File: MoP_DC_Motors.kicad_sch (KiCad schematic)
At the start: 21 parts, among them J18 Encoder1, J19 Encoder2, M3 1x2_Terminal, M4 1x2_Terminal, U4 L293D, U5 74AHCT1G14, U6 74AHCT1G14

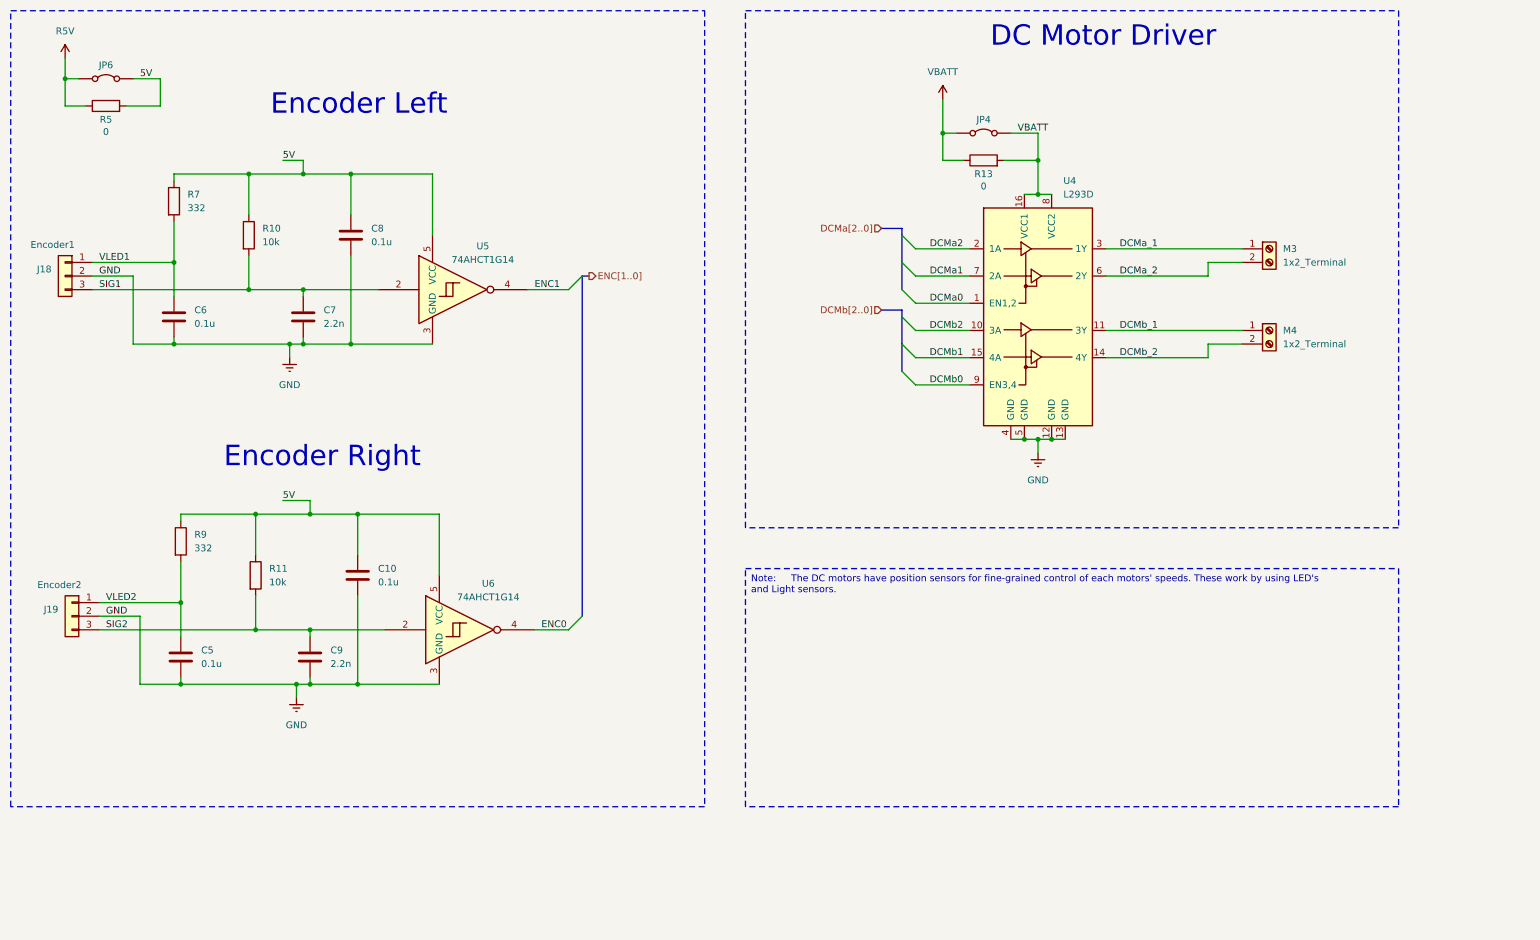
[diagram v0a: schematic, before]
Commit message: changed ref designators to be consistent accross sheets
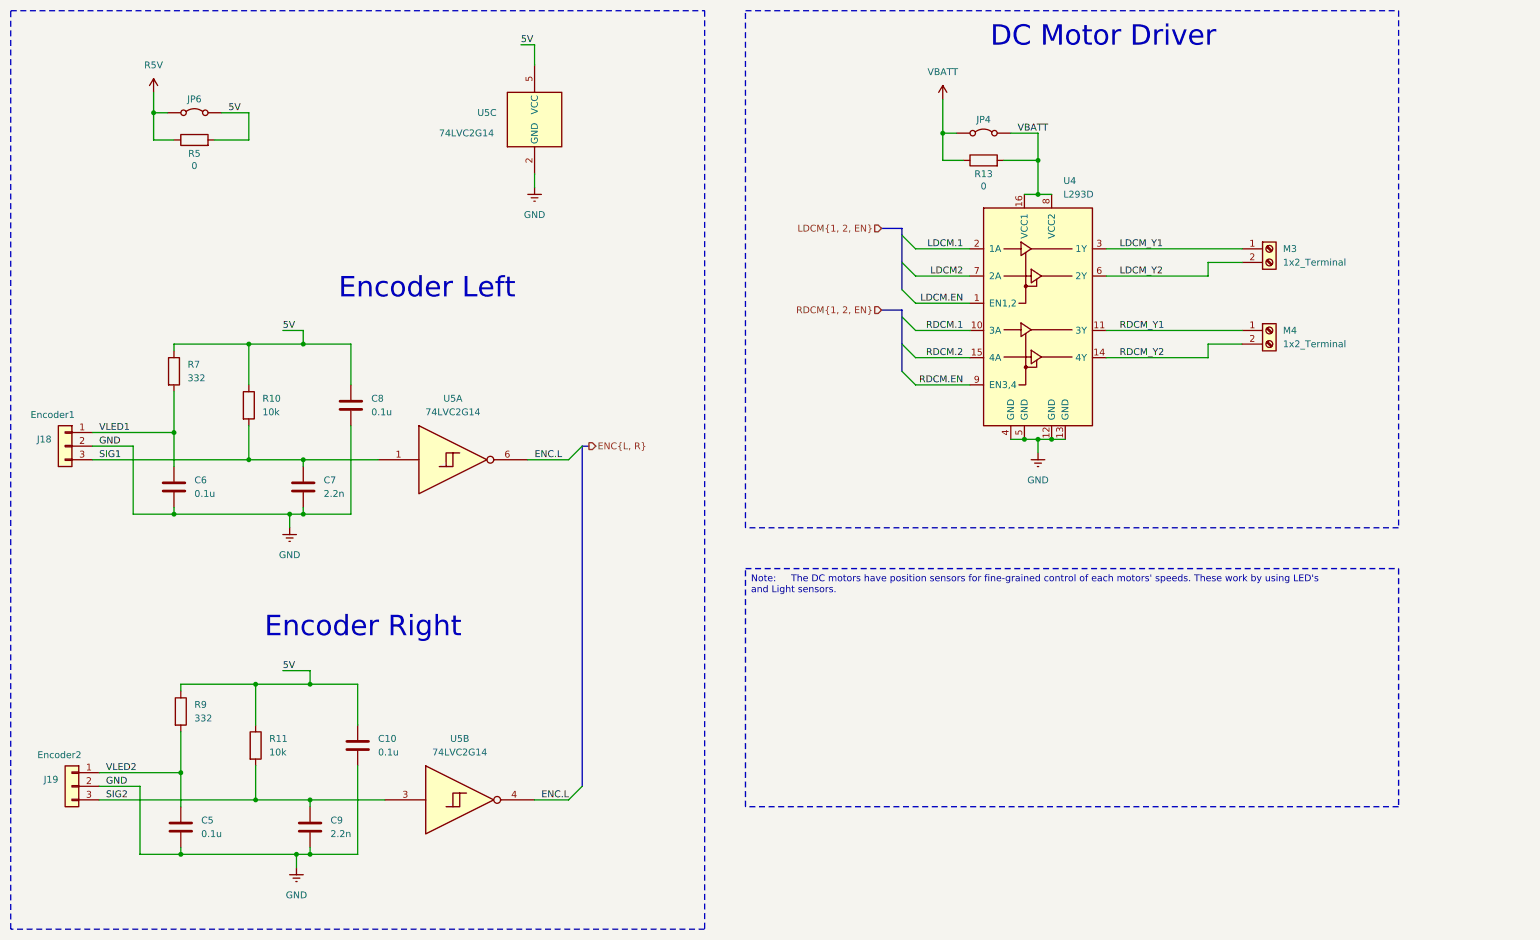
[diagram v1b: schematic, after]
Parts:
- removed U5, U6: 74AHCT1G14, symbol 74xGxx:74AHCT1G14
- added U5: 74LVC2G14, Package_TO_SOT_SMD:SOT-23-6, symbol 74xGxx:74LVC2G14
- C6, C7, C8: footprint (none) -> Capacitor_SMD:C_0805_2012Metric_Pad1.18x1.45mm_HandSolder
- R10, R7: footprint (none) -> Resistor_SMD:R_0805_2012Metric
- U4: footprint Package_DIP:DIP-20_W7.62mm_SMDSocket_SmallPads -> Package_DIP:DIP-16_W7.62mm_LongPads
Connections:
- net 5V: now also U5.5 (VCC)
- net GND: now also U5.2 (GND)
- net SIG1: now also U5.1
- net SIG2: now also U5.3
- net DCMa0 renamed LDCM.EN
- net DCMa1 renamed LDCM2
- net DCMa2 renamed LDCM.1
- net DCMa_1 renamed LDCM_Y1
- net DCMa_2 renamed LDCM_Y2
- net DCMb0 renamed RDCM.EN
- net DCMb1 renamed RDCM.2
- net DCMb2 renamed RDCM.1
- net DCMb_1 renamed RDCM_Y1
- net DCMb_2 renamed RDCM_Y2
- new net ENC.L: U5.4, U5.6
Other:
- moved on the sheet: C10, C5, C6, C7, C8, C9, J18, J19, JP6, R10, R11, R5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

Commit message: Finished schematics
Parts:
- C504: renamed from C10; footprint (none) -> Capacitor_SMD:C_0805_2012Metric_Pad1.18x1.45mm_HandSolder
- C505: renamed from C5; footprint (none) -> Capacitor_SMD:C_0805_2012Metric_Pad1.18x1.45mm_HandSolder
- C506: renamed from C9; footprint (none) -> Capacitor_SMD:C_0805_2012Metric_Pad1.18x1.45mm_HandSolder
- J501: renamed from J18; footprint (none) -> Connector_PinHeader_2.54mm:PinHeader_1x03_P2.54mm_Vertical
- J502: renamed from J19; footprint (none) -> Connector_PinHeader_2.54mm:PinHeader_1x03_P2.54mm_Vertical
- J503: renamed from M3; footprint (none) -> TerminalBlock_Phoenix:TerminalBlock_Phoenix_MKDS-1,5-2-5.08_1x02_P5.08mm_Horizontal
- J504: renamed from M4; footprint (none) -> TerminalBlock_Phoenix:TerminalBlock_Phoenix_MKDS-1,5-2-5.08_1x02_P5.08mm_Horizontal
- JP501: renamed from JP6; footprint (none) -> Connector_PinHeader_2.54mm:PinHeader_1x02_P2.54mm_Vertical
- JP502: renamed from JP4; footprint (none) -> Connector_PinHeader_2.54mm:PinHeader_1x02_P2.54mm_Vertical
- R501: renamed from R5; footprint (none) -> Resistor_SMD:R_0805_2012Metric; now not fitted
- R504: renamed from R9; footprint (none) -> Resistor_SMD:R_0805_2012Metric
- R505: renamed from R11; footprint (none) -> Resistor_SMD:R_0805_2012Metric
- R506: renamed from R13; footprint (none) -> Resistor_SMD:R_0805_2012Metric; now not fitted
- U4: footprint Package_DIP:DIP-16_W7.62mm_LongPads -> Package_DIP:DIP-16_W7.62mm_Socket_LongPads
- renumbered C8 to C501, C6 to C502, C7 to C503, R7 to R502, R10 to R503, U5 to U501
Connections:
- net VBATT: no longer JP502.2 (B), R506.2, U4.16 (VCC1), U4.8 (VCC2)
- new net VS: JP502.2 (B), R506.2, U4.16 (VCC1), U4.8 (VCC2)
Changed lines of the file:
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@@
 		)
 	)
-	(text_box "Note: 	The DC motors have position sensors for fine-grained control of each motors' speeds. These work by using LED's and Light sensors."
+	(text_box "Note: 	The DC motors have position sensors for fine-grained control of each motors' speeds. These work by using \n		LED's and Light sensors.\n\n		The L293D is a DIP-16 package that is installed via socket"
 		(exclude_from_sim no)
 		(at 156.21 123.19 0)
@@
 		)
 	)
-	(label "VBATT"
+	(label "VS"
 		(at 207.01 41.91 0)
 		(fields_autoplaced yes)
@@
 		(dnp no)
 		(fields_autoplaced yes)
-		(property "Reference" "R7"
+		(property "Reference" "R502"
 			(at 52.07 85.0899 0)
 			(effects
@@
 			(project "MoP"
 				(path "/4d76798e-9a11-4d8d-a723-72f274a89091/35a0f4f1-9888-4ee1-94e1-e8485c96600c"
-					(reference "R7")
+					(reference "R502")
 					(unit 1)
 				)
@@
 		(dnp no)
 		(fields_autoplaced yes)
-		(property "Reference" "C6"
+		(property "Reference" "C502"
 			(at 53.34 106.6799 0)
 			(effects
@@
 			(project "MoP"
 				(path "/4d76798e-9a11-4d8d-a723-72f274a89091/35a0f4f1-9888-4ee1-94e1-e8485c96600c"
-					(reference "C6")
+					(reference "C502")
 					(unit 1)
 				)
@@
 		(dnp no)
 		(fields_autoplaced yes)
-		(property "Reference" "R10"
+		(property "Reference" "R503"
 			(at 66.04 91.4399 0)
 			(effects
@@
 			(project "MoP"
 				(path "/4d76798e-9a11-4d8d-a723-72f274a89091/35a0f4f1-9888-4ee1-94e1-e8485c96600c"
-					(reference "R10")
+					(reference "R503")
 					(unit 1)
 				)
@@
 		(on_board yes)
 		(dnp no)
-		(property "Reference" "U5"
+		(property "Reference" "U501"
 			(at 107.95 38.1 0)
 			(effects
@@
 			(project "MoP"
 				(path "/4d76798e-9a11-4d8d-a723-72f274a89091/35a0f4f1-9888-4ee1-94e1-e8485c96600c"
-					(reference "U5")
+					(reference "U501")
 					(unit 3)
 				)
@@
 		(exclude_from_sim no)
 		(in_bom yes)
-		(on_board yes)
-		(dnp no)
-		(property "Reference" "R5"
+		(on_board no)
+		(dnp yes)
+		(property "Reference" "R501"
 			(at 53.34 45.72 90)
 			(effects
@@
 			)
 		)
-		(property "Footprint" ""
+		(property "Footprint" "Resistor_SMD:R_0805_2012Metric"
 			(at 53.34 44.958 90)
 			(effects
@@
 			(project "MoP"
 				(path "/4d76798e-9a11-4d8d-a723-72f274a89091/35a0f4f1-9888-4ee1-94e1-e8485c96600c"
-					(reference "R5")
+					(reference "R501")
 					(unit 1)
 				)
@@
 		(dnp no)
 		(fields_autoplaced yes)
-		(property "Reference" "U5"
+		(property "Reference" "U501"
 			(at 101.6 91.44 0)
 			(effects
@@
 			(project "MoP"
 				(path "/4d76798e-9a11-4d8d-a723-72f274a89091/35a0f4f1-9888-4ee1-94e1-e8485c96600c"
-					(reference "U5")
+					(reference "U501")
 					(unit 1)
 				)
@@
 		(dnp no)
 		(fields_autoplaced yes)
-		(property "Reference" "C5"
+		(property "Reference" "C505"
 			(at 54.61 170.1799 0)
 			(effects
@@
 			)
 		)
-		(property "Footprint" ""
+		(property "Footprint" "Capacitor_SMD:C_0805_2012Metric_Pad1.18x1.45mm_HandSolder"
 			(at 51.7652 175.26 0)
 			(effects
@@
 			(project "MoP"
 				(path "/4d76798e-9a11-4d8d-a723-72f274a89091/35a0f4f1-9888-4ee1-94e1-e8485c96600c"
-					(reference "C5")
+					(reference "C505")
 					(unit 1)
 				)
@@
 		(dnp no)
 		(fields_autoplaced yes)
-		(property "Reference" "M3"
+		(property "Reference" "J503"
 			(at 256.54 63.4999 0)
 			(effects
@@
 			)
 		)
-		(property "Footprint" ""
+		(property "Footprint" "TerminalBlock_Phoenix:TerminalBlock_Phoenix_MKDS-1,5-2-5.08_1x02_P5.08mm_Horizontal"
 			(at 254 63.5 0)
 			(effects
@@
 			(project "MoP"
 				(path "/4d76798e-9a11-4d8d-a723-72f274a89091/35a0f4f1-9888-4ee1-94e1-e8485c96600c"
-					(reference "M3")
+					(reference "J503")
 					(unit 1)
 				)
@@
 		(dnp no)
 		(fields_autoplaced yes)
-		(property "Reference" "JP4"
+		(property "Reference" "JP502"
 			(at 200.66 39.37 0)
 			(effects
@@
 			)
 		)
-		(property "Footprint" ""
+		(property "Footprint" "Connector_PinHeader_2.54mm:PinHeader_1x02_P2.54mm_Vertical"
 			(at 200.66 41.91 0)
 			(effects
@@
 			(project "MoP"
 				(path "/4d76798e-9a11-4d8d-a723-72f274a89091/35a0f4f1-9888-4ee1-94e1-e8485c96600c"
-					(reference "JP4")
+					(reference "JP502")
 					(unit 1)
 				)
@@
 		(dnp no)
 		(fields_autoplaced yes)
-		(property "Reference" "M4"
+		(property "Reference" "J504"
 			(at 256.54 78.7399 0)
 			(effects
@@
 			)
 		)
-		(property "Footprint" ""
+		(property "Footprint" "TerminalBlock_Phoenix:TerminalBlock_Phoenix_MKDS-1,5-2-5.08_1x02_P5.08mm_Horizontal"
 			(at 254 78.74 0)
 			(effects
@@
 			(project "MoP"
 				(path "/4d76798e-9a11-4d8d-a723-72f274a89091/35a0f4f1-9888-4ee1-94e1-e8485c96600c"
-					(reference "M4")
+					(reference "J504")
 					(unit 1)
 				)
@@
 		(dnp no)
 		(fields_autoplaced yes)
-		(property "Reference" "C8"
+		(property "Reference" "C501"
 			(at 86.36 91.4399 0)
 			(effects
@@
 			(project "MoP"
 				(path "/4d76798e-9a11-4d8d-a723-72f274a89091/35a0f4f1-9888-4ee1-94e1-e8485c96600c"
-					(reference "C8")
+					(reference "C501")
 					(unit 1)
 				)
@@
 		(dnp no)
 		(fields_autoplaced yes)
-		(property "Reference" "U5"
+		(property "Reference" "U501"
 			(at 102.87 154.94 0)
 			(effects
@@
 			(project "MoP"
 				(path "/4d76798e-9a11-4d8d-a723-72f274a89091/35a0f4f1-9888-4ee1-94e1-e8485c96600c"
-					(reference "U5")
+					(reference "U501")
 					(unit 2)
 				)
@@
 		(dnp no)
 		(fields_autoplaced yes)
-		(property "Reference" "R9"
+		(property "Reference" "R504"
 			(at 53.34 148.5899 0)
 			(effects
@@
 			)
 		)
-		(property "Footprint" ""
+		(property "Footprint" "Resistor_SMD:R_0805_2012Metric"
 			(at 49.022 149.86 90)
 			(effects
@@
 			(project "MoP"
 				(path "/4d76798e-9a11-4d8d-a723-72f274a89091/35a0f4f1-9888-4ee1-94e1-e8485c96600c"
-					(reference "R9")
+					(reference "R504")
 					(unit 1)
 				)
@@
 		(dnp no)
 		(fields_autoplaced yes)
-		(property "Reference" "C10"
+		(property "Reference" "C504"
 			(at 87.63 154.9399 0)
 			(effects
@@
 			)
 		)
-		(property "Footprint" ""
+		(property "Footprint" "Capacitor_SMD:C_0805_2012Metric_Pad1.18x1.45mm_HandSolder"
 			(at 84.7852 160.02 0)
 			(effects
@@
 			(project "MoP"
 				(path "/4d76798e-9a11-4d8d-a723-72f274a89091/35a0f4f1-9888-4ee1-94e1-e8485c96600c"
-					(reference "C10")
+					(reference "C504")
 					(unit 1)
 				)
@@
 		(on_board yes)
 		(dnp no)
-		(property "Reference" "J19"
+		(property "Reference" "J502"
 			(at 27.94 162.5599 0)
 			(effects
@@
 			)
 		)
-		(property "Footprint" ""
+		(property "Footprint" "Connector_PinHeader_2.54mm:PinHeader_1x03_P2.54mm_Vertical"
 			(at 30.48 163.83 0)
 			(effects
@@
 			(project "MoP"
 				(path "/4d76798e-9a11-4d8d-a723-72f274a89091/35a0f4f1-9888-4ee1-94e1-e8485c96600c"
-					(reference "J19")
+					(reference "J502")
 					(unit 1)
 				)
@@
 			)
 		)
-		(property "Footprint" "Package_DIP:DIP-16_W7.62mm_LongPads"
+		(property "Footprint" "Package_DIP:DIP-16_W7.62mm_Socket_LongPads"
 			(at 217.17 97.79 0)
 			(effects
@@
 		(dnp no)
 		(fields_autoplaced yes)
-		(property "Reference" "R11"
+		(property "Reference" "R505"
 			(at 67.31 154.9399 0)
 			(effects
@@
 			)
 		)
-		(property "Footprint" ""
+		(property "Footprint" "Resistor_SMD:R_0805_2012Metric"
 			(at 62.992 156.21 90)
 			(effects
@@
 			(project "MoP"
 				(path "/4d76798e-9a11-4d8d-a723-72f274a89091/35a0f4f1-9888-4ee1-94e1-e8485c96600c"
-					(reference "R11")
+					(reference "R505")
 					(unit 1)
 				)
@@
 		(dnp no)
 		(fields_autoplaced yes)
-		(property "Reference" "JP6"
+		(property "Reference" "JP501"
 			(at 53.34 35.56 0)
 			(effects
@@
 			)
 		)
-		(property "Footprint" ""
+		(property "Footprint" "Connector_PinHeader_2.54mm:PinHeader_1x02_P2.54mm_Vertical"
 			(at 53.34 38.1 0)
 			(effects
@@
 			(project "MoP"
 				(path "/4d76798e-9a11-4d8d-a723-72f274a89091/35a0f4f1-9888-4ee1-94e1-e8485c96600c"
-					(reference "JP6")
+					(reference "JP501")
 					(unit 1)
 				)
@@
 		(exclude_from_sim no)
 		(in_bom yes)
-		(on_board yes)
-		(dnp no)
-		(property "Reference" "R13"
+		(on_board no)
+		(dnp yes)
+		(property "Reference" "R506"
+			(at 200.66 44.196 90)
+			(effects
+				(font
+					(size 1.27 1.27)
+				)
+			)
+		)
+		(property "Value" "0"
 			(at 200.66 49.53 90)
 			(effects
@@
 			)
 		)
-		(property "Value" "0"
-			(at 200.66 51.816 90)
-			(effects
-				(font
-					(size 1.27 1.27)
-				)
-			)
-		)
-		(property "Footprint" ""
+		(property "Footprint" "Resistor_SMD:R_0805_2012Metric"
 			(at 200.66 48.768 90)
 			(effects
@@
 			(project "MoP"
 				(path "/4d76798e-9a11-4d8d-a723-72f274a89091/35a0f4f1-9888-4ee1-94e1-e8485c96600c"
-					(reference "R13")
+					(reference "R506")
 					(unit 1)
 				)
@@
 		(dnp no)
 		(fields_autoplaced yes)
-		(property "Reference" "C7"
+		(property "Reference" "C503"
 			(at 77.47 106.6799 0)
 			(effects
@@
 			(project "MoP"
 				(path "/4d76798e-9a11-4d8d-a723-72f274a89091/35a0f4f1-9888-4ee1-94e1-e8485c96600c"
-					(reference "C7")
+					(reference "C503")
 					(unit 1)
 				)
@@
 		(on_board yes)
 		(dnp no)
-		(property "Reference" "J18"
+		(property "Reference" "J501"
 			(at 26.67 99.0599 0)
 			(effects
@@
 			)
 		)
-		(property "Footprint" ""
+		(property "Footprint" "Connector_PinHeader_2.54mm:PinHeader_1x03_P2.54mm_Vertical"
 			(at 29.21 100.33 0)
 			(effects
@@
 			(project ""
 				(path "/4d76798e-9a11-4d8d-a723-72f274a89091/35a0f4f1-9888-4ee1-94e1-e8485c96600c"
-					(reference "J18")
+					(reference "J501")
 					(unit 1)
 				)
@@
 		(dnp no)
 		(fields_autoplaced yes)
-		(property "Reference" "C9"
+		(property "Reference" "C506"
 			(at 78.74 170.1799 0)
 			(effects
@@
 			)
 		)
-		(property "Footprint" ""
+		(property "Footprint" "Capacitor_SMD:C_0805_2012Metric_Pad1.18x1.45mm_HandSolder"
 			(at 75.8952 175.26 0)
 			(effects
@@
 			(project "MoP"
 				(path "/4d76798e-9a11-4d8d-a723-72f274a89091/35a0f4f1-9888-4ee1-94e1-e8485c96600c"
-					(reference "C9")
-					(unit 1)
-				)
+					(reference "C506")
+					(unit 1)
+				)
